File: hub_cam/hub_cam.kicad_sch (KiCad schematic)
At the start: 17 parts, among them J1 IMU 1x4 P2.54, J2 CAM1 GH-4, J3 CAM2 GH-4, J4 HOST VBUS, J5 HOST DM, J6 HOST DP, J7 HOST GND, U1 FE1.1S-BQFN24B, Y1 12MHz

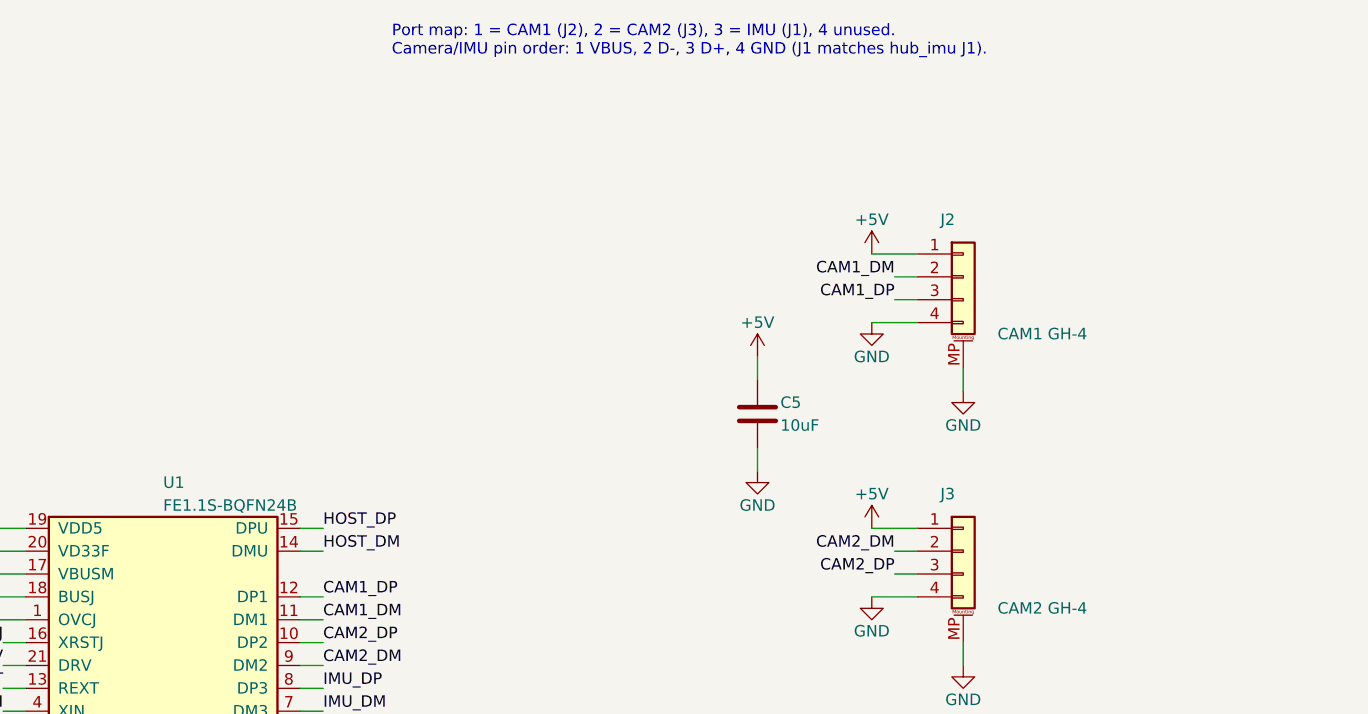
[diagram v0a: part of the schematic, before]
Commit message: hub_cam: add USBLC6-2SC6 ESD protection at both camera connectors
Co-Authored-By: Claude Opus 5.5 <noreply@anthropic.com>
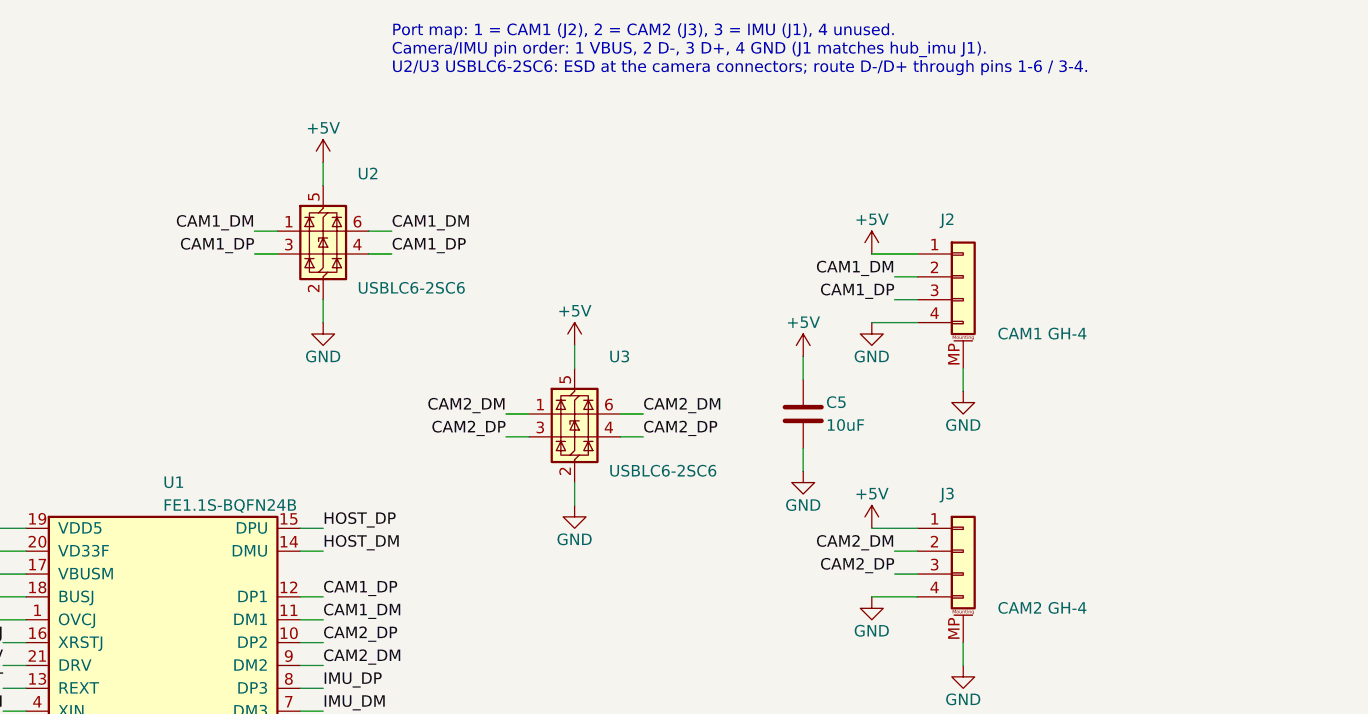
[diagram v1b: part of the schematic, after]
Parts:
- added U2, U3: USBLC6-2SC6, Package_TO_SOT_SMD:SOT-23-6, symbol hubcam:USBLC6-2SC6
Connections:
- net +5V: now also U2.5 (VBUS), U3.5 (VBUS)
- net CAM1_DM: now also U2.1 (I/O1), U2.6 (I/O1)
- net CAM1_DP: now also U2.3 (I/O2), U2.4 (I/O2)
- net CAM2_DM: now also U3.1 (I/O1), U3.6 (I/O1)
- net CAM2_DP: now also U3.3 (I/O2), U3.4 (I/O2)
- net GND: now also U2.2 (GND), U3.2 (GND)
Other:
- note added: "Port map: 1 = CAM1 (J2), 2 = CAM2 (J3), 3 = IMU (J1), 4 unused. Camera/IMU pin order: 1 VBUS, 2 D-, 3 D+, 4 GND (J1 matches hub_imu J1). U2/U3 USBLC6-2SC6: ESD at the camera connectors; route D-/D+ through pins 1-6 / 3-4."
- note removed: "Port map: 1 = CAM1 (J2), 2 = CAM2 (J3), 3 = IMU (J1), 4 unused. Camera/IMU pin order: 1 VBUS, 2 D-, 3 D+, 4 GND (J1 matches hub_imu J1)."

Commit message: hub_cam: PCB layout with USB-C host port and JST SH camera ports
- Host: USB-C receptacle J4 (C2765186) with 5.1k CC pull-downs R4/R5,
  plus backup wire pads J5-J8 (5V, D+, D-, GND) on the back.
- Cameras: JST SH SM04B-SRSS-TB (C160404) replaces JST GH.
- Board 31.66 x 16.65 mm, 1.0 mm, 2 layers, single-sided SMD assembly.
- Six 1.4 mm thread holes: four on the camera shelf, two beside the USB-C.
- J1 (IMU stacking header) marked DNP.
- Silkscreen: refs hidden, CAM1/CAM2 and wire-pad labels added.
- DRC: 0 errors, 0 unconnected. README, renders and dimensions updated.

Co-Authored-By: Claude Opus 5.5 <noreply@anthropic.com>
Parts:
- removed J4: HOST VBUS, Connector_Wire:SolderWire-1.5sqmm_1x01_D1.7mm_OD3mm, symbol hubcam:Conn_01x01
- added J4: HOST USB-C, Connector_USB:USB_C_Receptacle_GCT_USB4105-xx-A_16P_TopMnt_Horizontal, symbol hubcam:USB_C_Receptacle_USB2.0_16P
- added J8: HOST GND, Connector_Wire:SolderWirePad_1x01_SMD_1.5x3mm, symbol hubcam:Conn_01x01
- added R4, R5: 5.1k, Resistor_SMD:R_0402_1005Metric, symbol hubcam:R
- J1: now not fitted
- J2: value CAM1 GH-4 -> CAM1 SH-4; footprint Connector_JST:JST_GH_SM04B-GHS-TB_1x04-1MP_P1.25mm_Horizontal -> Connector_JST:JST_SH_SM04B-SRSS-TB_1x04-1MP_P1.00mm_Horizontal; JLCPCB Part # C189895 -> C160404
- J3: value CAM2 GH-4 -> CAM2 SH-4; footprint Connector_JST:JST_GH_SM04B-GHS-TB_1x04-1MP_P1.25mm_Horizontal -> Connector_JST:JST_SH_SM04B-SRSS-TB_1x04-1MP_P1.00mm_Horizontal; JLCPCB Part # C189895 -> C160404
- J5: value HOST DM -> HOST VBUS; footprint Connector_Wire:SolderWire-0.25sqmm_1x01_D0.65mm_OD1.7mm -> Connector_Wire:SolderWirePad_1x01_SMD_1.5x3mm
- J6: value HOST DP -> HOST DM; footprint Connector_Wire:SolderWire-0.25sqmm_1x01_D0.65mm_OD1.7mm -> Connector_Wire:SolderWirePad_1x01_SMD_1.5x3mm
- J7: value HOST GND -> HOST DP; footprint Connector_Wire:SolderWire-1.5sqmm_1x01_D1.7mm_OD3mm -> Connector_Wire:SolderWirePad_1x01_SMD_1.5x3mm
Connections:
- net +5V: now also J5.1 (Pin_1), J4.A4 (VBUS), J4.A9 (VBUS), J4.B4 (VBUS), J4.B9 (VBUS)
- net CAM2_DM: now also U1.7 (DM3); no longer U1.9 (DM2)
- net CAM2_DP: now also U1.8 (DP3); no longer U1.10 (DP2)
- net GND: now also J4.A1 (GND), J4.A12 (GND), J4.B1 (GND), J4.B12 (GND), J4.S1 (SHIELD), J8.1 (Pin_1), R4.2, R5.2; no longer J7.1 (Pin_1)
- net HOST_DM: now also J6.1 (Pin_1), J4.A7 (D-), J4.B7 (D-); no longer J5.1 (Pin_1)
- net HOST_DP: now also J7.1 (Pin_1), J4.A6 (D+), J4.B6 (D+); no longer J6.1 (Pin_1)
- net IMU_DM: now also U1.9 (DM2); no longer U1.7 (DM3)
- net IMU_DP: now also U1.10 (DP2); no longer U1.8 (DP3)
- new net CC1: J4.A5 (CC1), R4.1
- new net CC2: J4.B5 (CC2), R5.1
- no-connect marks 6 -> 8
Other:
- note added: "Host: USB-C receptacle, USB 2.0 only. R4/R5 5.1k CC pull-downs identify a sink/device so C-to-C cables supply VBUS. Shield tied to GND. SBU unused."
- note added: "J5-J8: backup host wire pads on the back (hand-soldered), in parallel with J4. Leave J4/R4/R5 off the BOM if wires are used."
- note added: "Port map: 1 = CAM1 (J2), 2 = IMU (J1), 3 = CAM2 (J3), 4 unused. Camera/IMU pin order: 1 VBUS, 2 D-, 3 D+, 4 GND (J1 matches hub_imu J1). U2/U3 USBLC6-2SC6: ESD at the camera connectors; route D-/D+ through pins 1-6 / 3-4."
- note removed: "Host cable: J4/J7 1.7 mm holes for 16-18 AWG power, J5/J6 0.65 mm holes for data."
- note removed: "Port map: 1 = CAM1 (J2), 2 = CAM2 (J3), 3 = IMU (J1), 4 unused. Camera/IMU pin order: 1 VBUS, 2 D-, 3 D+, 4 GND (J1 matches hub_imu J1). U2/U3 USBLC6-2SC6: ESD at the camera connectors; route D-/D+ through pins 1-6 / 3-4."
